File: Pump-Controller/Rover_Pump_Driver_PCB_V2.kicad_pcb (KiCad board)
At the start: 2 copper layers, 3 parts

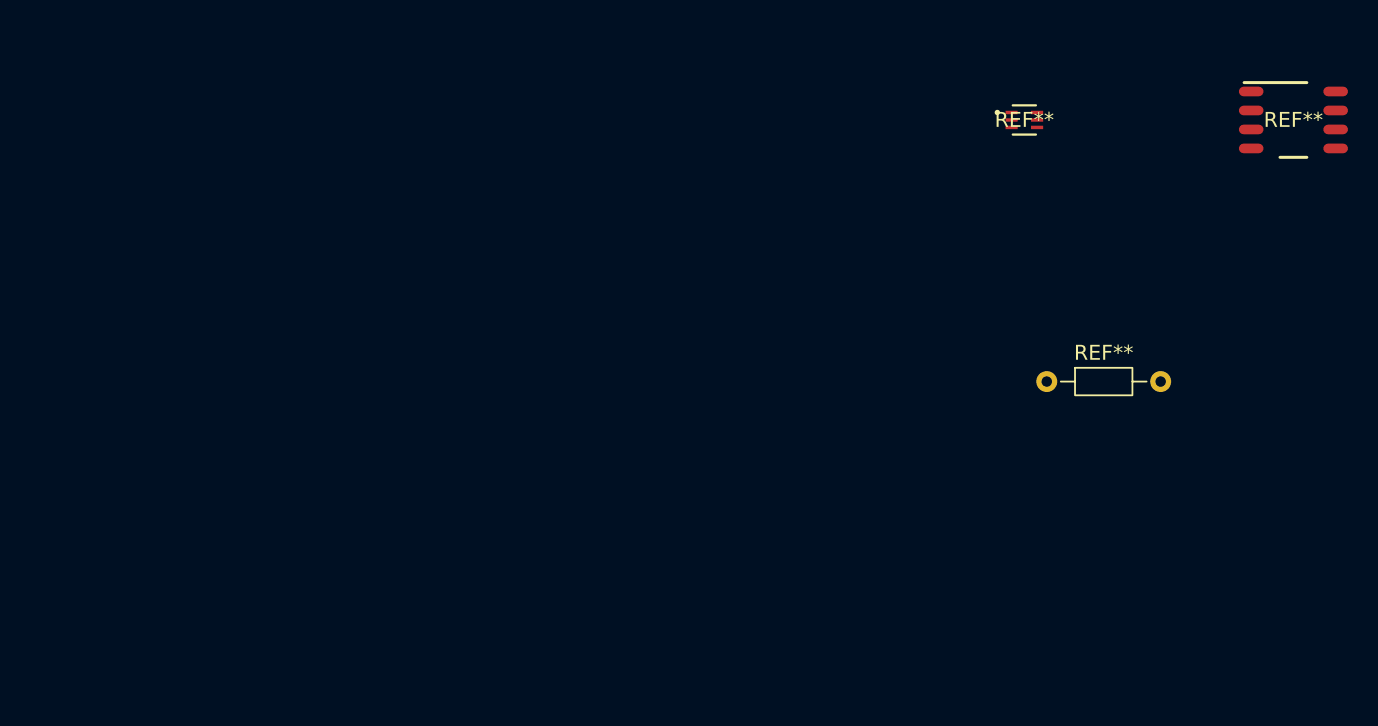
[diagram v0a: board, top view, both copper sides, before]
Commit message: Update to Pump Driver Board.  First draft of PCB layout finished.
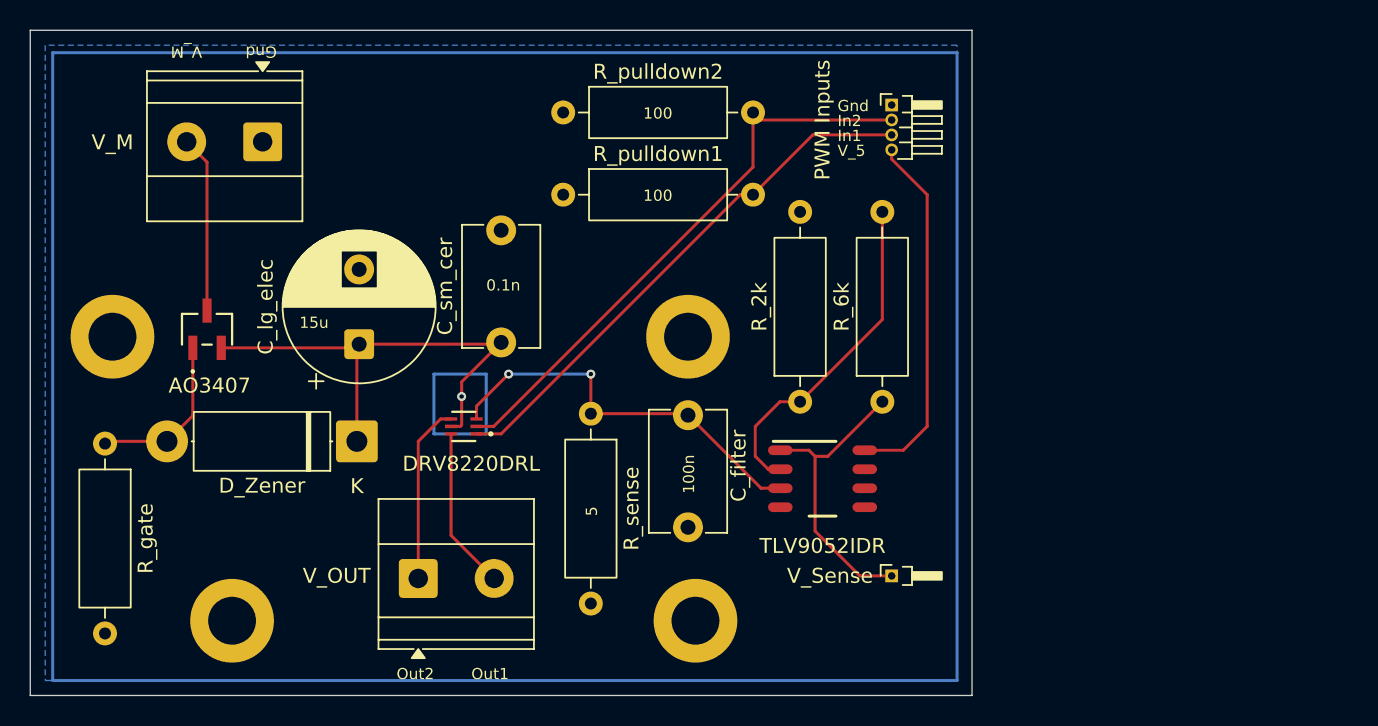
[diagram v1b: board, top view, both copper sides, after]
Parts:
- removed the REF** at (158.0, 107.5)
- removed the REF** at (156.5, 90.0)
- added AO3407: SOT-23-3L_AOS, AO3407A:SOT-23-3L_AOS-M, F.Cu at (101.8, 104.0)
- added C_filter: C_Disc_D8.0mm_W5.0mm_P7.50mm, Capacitor_THT:C_Disc_D8.0mm_W5.0mm_P7.50mm, F.Cu at (134.0, 109.8)
- added C_lg_elec: CP_Radial_D10.0mm_P5.00mm, Capacitor_THT:CP_Radial_D10.0mm_P5.00mm, F.Cu at (112.0, 105.0)
- added C_sm_cer: C_Disc_D8.0mm_W5.0mm_P7.50mm, Capacitor_THT:C_Disc_D8.0mm_W5.0mm_P7.50mm, F.Cu at (121.5, 104.9)
- added DRV8220DRL: SOT5X3-6_DRL_TEX, footprints:SOT5X3-6_DRL_TEX-M, F.Cu at (119.0, 110.5)
- added D_Zener: D_5W_P12.70mm_Horizontal, Diode_THT:D_5W_P12.70mm_Horizontal, F.Cu at (111.8, 111.5)
- added PWM Inputs: PinHeader_1x04_P1.00mm_Horizontal, Connector_PinHeader_1.00mm:PinHeader_1x04_P1.00mm_Horizontal, F.Cu at (147.6, 89.0)
- added REF**: MountingHole_3.2mm_M3_DIN965_Pad, MountingHole:MountingHole_3.2mm_M3_DIN965_Pad, F.Cu at (134.5, 123.5)
- added REF**: MountingHole_3.2mm_M3_DIN965_Pad, MountingHole:MountingHole_3.2mm_M3_DIN965_Pad, F.Cu at (134.0, 104.5)
- added REF**: MountingHole_3.2mm_M3_DIN965_Pad, MountingHole:MountingHole_3.2mm_M3_DIN965_Pad, F.Cu at (103.5, 123.5)
- added REF**: MountingHole_3.2mm_M3_DIN965_Pad, MountingHole:MountingHole_3.2mm_M3_DIN965_Pad, F.Cu at (95.5, 104.5)
- added R_2k: R_Axial_DIN0309_L9.0mm_D3.2mm_P12.70mm_Horizontal, Resistor_THT:R_Axial_DIN0309_L9.0mm_D3.2mm_P12.70mm_Horizontal, F.Cu at (141.5, 108.8)
- added R_6k: R_Axial_DIN0309_L9.0mm_D3.2mm_P12.70mm_Horizontal, Resistor_THT:R_Axial_DIN0309_L9.0mm_D3.2mm_P12.70mm_Horizontal, F.Cu at (147.0, 108.8)
- added R_gate: R_Axial_DIN0309_L9.0mm_D3.2mm_P12.70mm_Horizontal, Resistor_THT:R_Axial_DIN0309_L9.0mm_D3.2mm_P12.70mm_Horizontal, F.Cu at (95.0, 111.7)
- added R_pulldown1: R_Axial_DIN0309_L9.0mm_D3.2mm_P12.70mm_Horizontal, Resistor_THT:R_Axial_DIN0309_L9.0mm_D3.2mm_P12.70mm_Horizontal, F.Cu at (125.7, 95.0)
- added R_pulldown2: R_Axial_DIN0309_L9.0mm_D3.2mm_P12.70mm_Horizontal, Resistor_THT:R_Axial_DIN0309_L9.0mm_D3.2mm_P12.70mm_Horizontal, F.Cu at (125.7, 89.5)
- added R_sense: R_Axial_DIN0309_L9.0mm_D3.2mm_P12.70mm_Horizontal, Resistor_THT:R_Axial_DIN0309_L9.0mm_D3.2mm_P12.70mm_Horizontal, F.Cu at (127.5, 109.7)
- added V_M: TerminalBlock_Phoenix_MKDS-1,5-2-5.08_1x02_P5.08mm_Horizont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, TerminalBlock_Phoenix:TerminalBlock_Phoenix_MKDS-1,5-2-5.08_1x02_P5.08mm_Horizontal, F.Cu at (105.5, 91.5)
- added V_OUT: TerminalBlock_Phoenix_MKDS-1,5-2-5.08_1x02_P5.08mm_Horizont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, TerminalBlock_Phoenix:TerminalBlock_Phoenix_MKDS-1,5-2-5.08_1x02_P5.08mm_Horizontal, F.Cu at (116.0, 120.7)
- added V_Sense: PinHeader_1x01_P1.00mm_Horizontal, Connector_PinHeader_1.00mm:PinHeader_1x01_P1.00mm_Horizontal, F.Cu at (147.6, 120.5)
- moved TLV9052IDR 39.6 mm to (143.0, 114.0)
- renumbered REF** to TLV9052IDR
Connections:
- TLV9052IDR pad 1: (no net) -> V_sense
- TLV9052IDR pad 2: (no net) -> V_sense
- TLV9052IDR pad 3: (no net) -> V_sense_in
- TLV9052IDR pad 4: (no net) -> gnd
- TLV9052IDR pad 8: (no net) -> V_5
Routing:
- net V_M: track 0.00 -> 44.7 mm, vias 0 -> 1
- net V_sense: track 0.00 -> 42.6 mm
- net in2: track 0.00 -> 38.8 mm
- net in1: track 0.00 -> 36.1 mm
- net V_sense_in: track 0.00 -> 26.8 mm, vias 0 -> 2
- net V_5: track 0.00 -> 24.3 mm
- net out2: track 0.00 -> 12.0 mm
- net V_z: track 0.00 -> 11.2 mm
- net out1: track 0.00 -> 10.9 mm
- added copper zone on B.Cu, net V_M
- added copper zone on B.Cu, net gnd
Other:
- board outline added: 63 x 44.5 mm
- board text added: "0.1n"
- board text added: "100"
- board text added: "100n"
- board text added: "15u"
- board text added: "5"
- board text added: "Gnd"
- board text added: "In1"
- board text added: "In2"
- board text added: "Out1"
- board text added: "Out2"
- board text added: "V_5"
- board text added: "V_M"
